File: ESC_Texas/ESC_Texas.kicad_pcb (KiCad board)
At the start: 4 copper layers, 118 x 73.2 mm, 151 parts, among them IC1 nRF52840-QFAA-F-R7, IC10 UCC21331CQDRQ1, IC11 LM3480IM3-3.3_NOPB, IC2 UCC21331CQDRQ1, IC3 AD8411AWBRZ, IC4 MC78L05ACHT1G, IC5 AD8411AWBRZ, IC6 MC78L05ACHT1G, IC7 UCC21331CQDRQ1, IC8 AD8411AWBRZ, IC9 MC78L05ACHT1G, J1 Battery, J10 Conn_01x03_Pin, J11 Conn_01x02_Pin, J13 Conn_01x06_Pin, J14 Conn_01x04_Pin, J15 Conn_01x04_Pin, J16 Conn_01x07_Pin, J2 Conn_01x08_Pin, J3 Motor, J5 Conn_01x03_Pin, J6 Conn_01x03_Pin, J7 Conn_01x03_Pin, J8 Conn_01x03_Pin, J9 Conn_01x03_Pin, Q1 IPD100N06S4, Q2 IPD100N06S4, Q3 IPD100N06S4, Q4 IPD100N06S4, Q5 IPD100N06S4, Q6 IPD100N06S4, Y1 CM7V-T1A-32.768kHz, Y2 32MHz

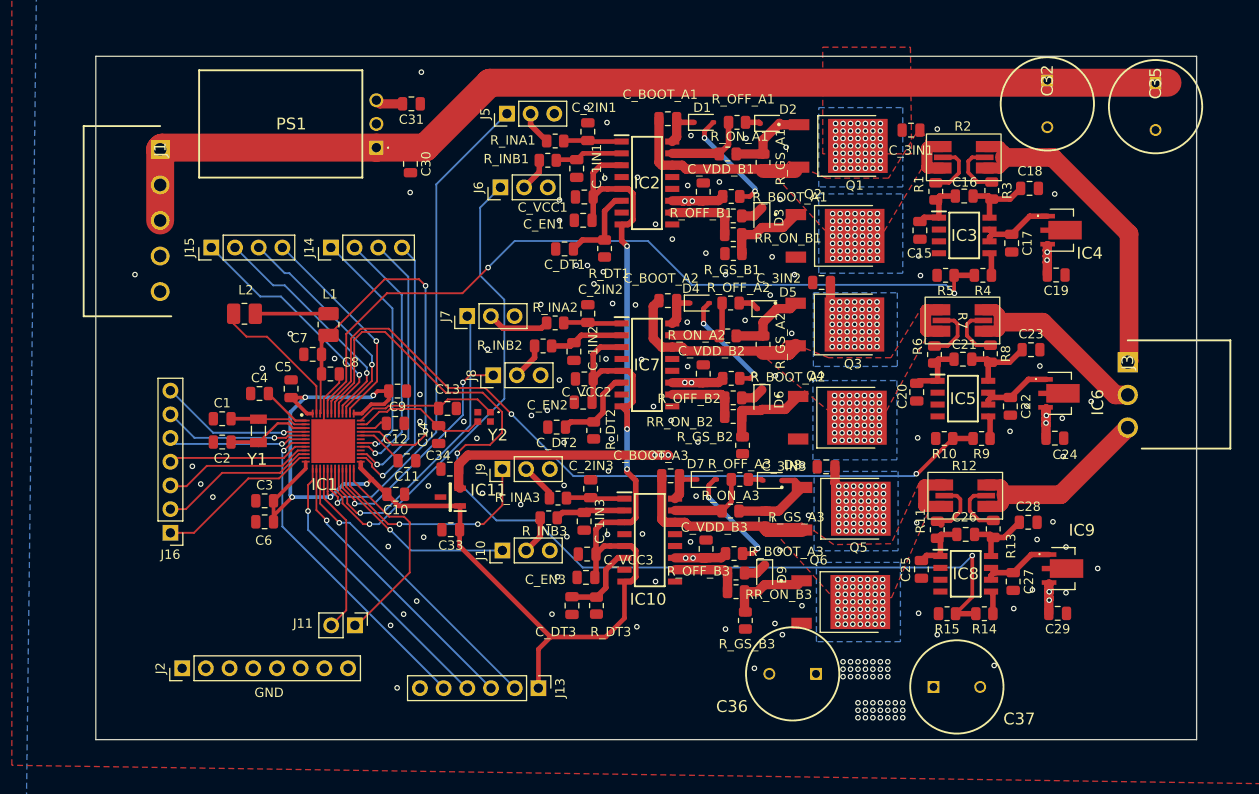
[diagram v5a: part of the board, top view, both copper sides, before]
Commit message: Mounting holes and bettery connection added
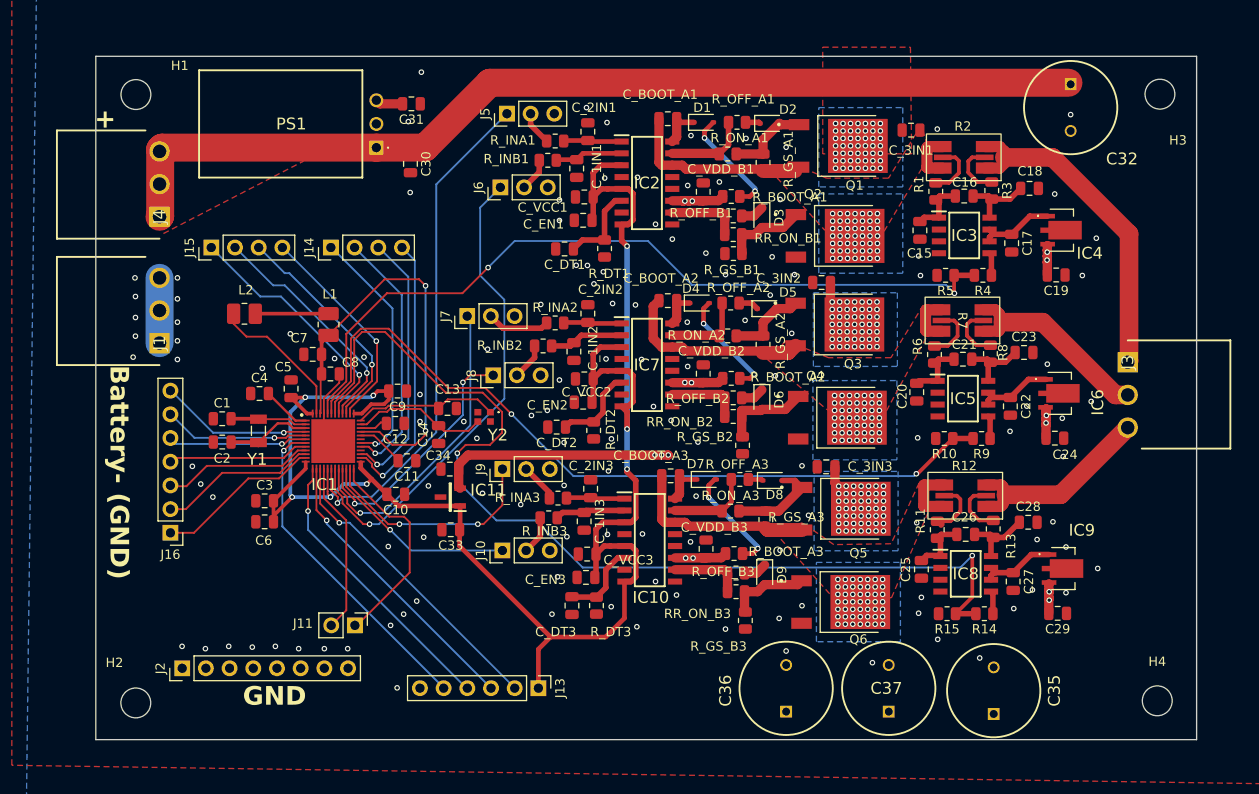
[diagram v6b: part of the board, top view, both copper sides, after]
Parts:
- added H1: MountingHole, MountingHole:MountingHole_3.2mm_M3, F.Cu at (96.3, 78.1)
- added H2: MountingHole, MountingHole:MountingHole_3.2mm_M3, F.Cu at (96.3, 143.3)
- added H3: MountingHole, MountingHole:MountingHole_3.2mm_M3, F.Cu at (206.1, 78.1)
- added H4: MountingHole, MountingHole:MountingHole_3.2mm_M3, F.Cu at (205.8, 143.1)
- added J4: Battery+, LIB_2350514-3:SHDRRA3W90P0X350_1X3_1110X920X691P, F.Cu at (98.8, 91.2)
- J1: value Battery -> Battery-; footprint 691322310005:SHDRRA5W80P0X381_1X5_2024X920X720P -> LIB_2350514-3:SHDRRA3W90P0X350_1X3_1110X920X691P
- moved C35 69.8 mm to (188.2, 144.5), turned to 90 degrees
- moved J1 20.8 mm to (98.8, 104.8)
- moved C37 5.48 mm to (177.0, 144.2), turned to 90 degrees
- moved C36 5.16 mm to (166.0, 144.2), turned to 90 degrees
- moved C32 2.53 mm to (196.5, 77.0)
- moved C23 0.81 mm to (191.5, 105.8)
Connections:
- J1 pad 1: +36V -> GND
- J1 pad 2: +36V -> GND
- J1 pad 3: +36V -> GND
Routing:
- net GND: track 8.30 -> 15.3 mm, vias 105 -> 130
- net +36V: track 224.7 -> 229.9 mm, vias 189 -> 147
- net Net-(IC5-+IN): track 8.26 -> 7.38 mm
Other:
- board text added: "+"
- board text added: "Battery- (GND)"

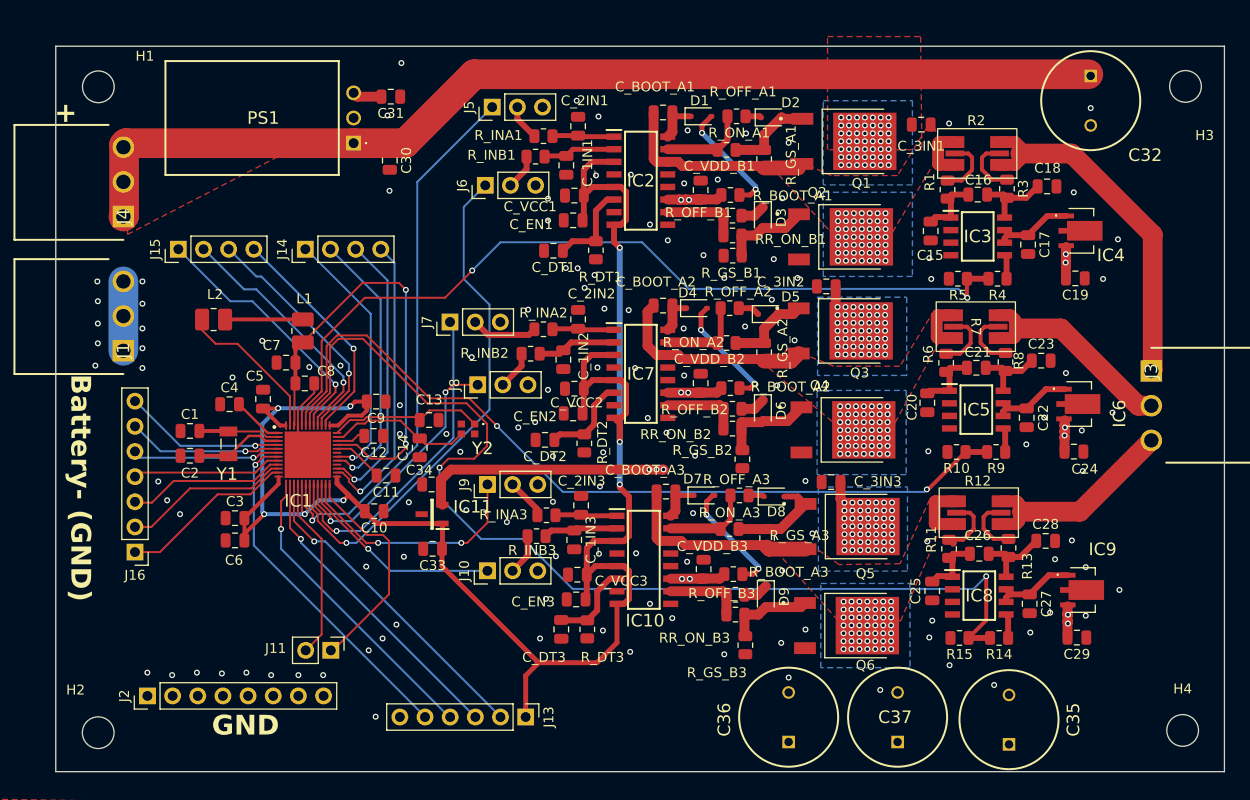
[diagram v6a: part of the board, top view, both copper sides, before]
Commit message: Starting to edit nRF footprint for smaller paste pads
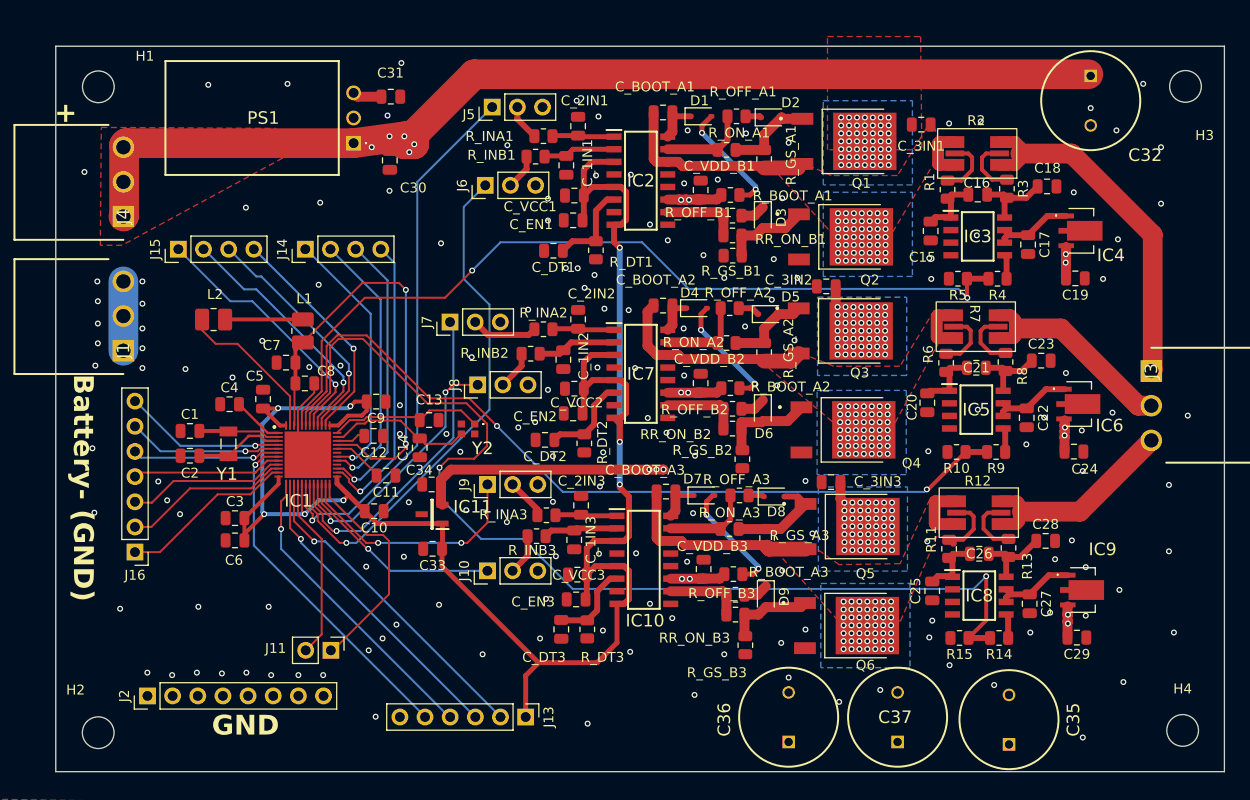
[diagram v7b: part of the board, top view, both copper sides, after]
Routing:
- net +36V: track 229.9 -> 230.5 mm, vias 147 -> 152
- net GND: vias 130 -> 162
